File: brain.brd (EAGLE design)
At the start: 100 x 80 mm, 14 parts

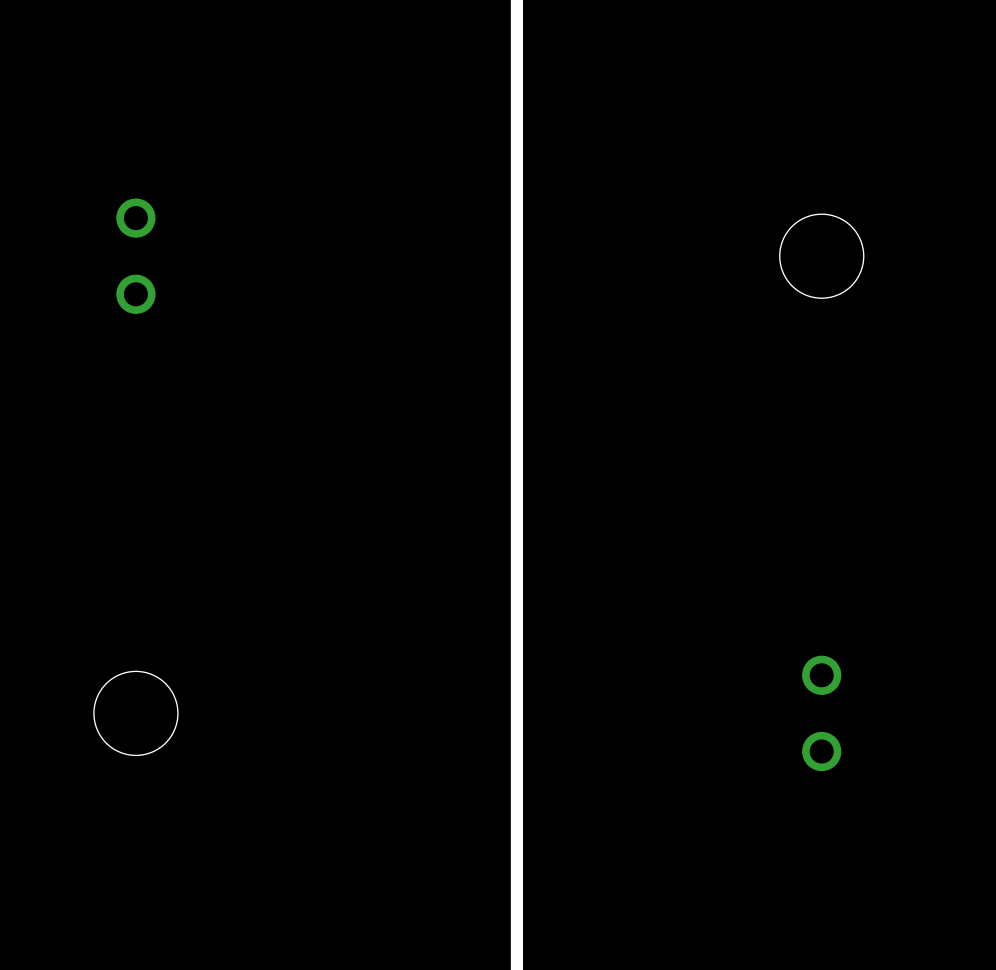
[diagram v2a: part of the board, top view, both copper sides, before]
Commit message: Added some text to board, played a bit with layout/routing.
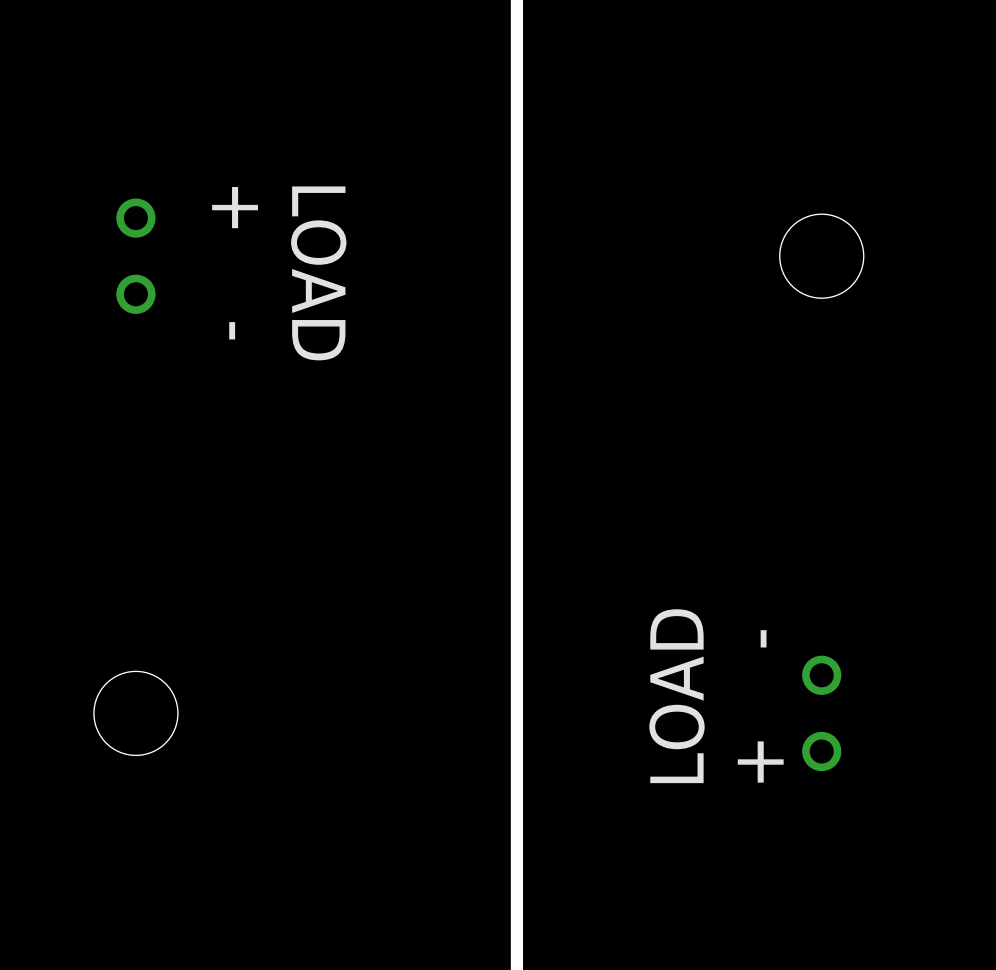
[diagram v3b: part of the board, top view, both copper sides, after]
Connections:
- removed net +3V3: U$1.8, U$2.VOUT, U$4.8, U$5.VOUT, XB1.1, XB2.1
- removed net GND: R1.2, R2.2, S1.2, S2.2, U$1.4, U$2.GND, U$3.P$2, U$4.4, U$5.GND, U$6.P$2, XB1.10, XB2.10
- removed net VIN: U$2.VIN, U$3.P$1, U$5.VIN, U$6.P$1
- new net GND1: R1.2, R2.2, S1.2, U$1.4, U$2.GND, U$3.P$2, XB1.10
- new net GND2: S2.2, U$4.4, U$5.GND, U$6.P$2, XB2.10
- new net VCC1: U$1.8, U$2.VOUT, XB1.1
- new net VIN1: U$2.VIN, U$3.P$1
- new net VIN2: U$5.VIN, U$6.P$1
- new net VOUT2: U$4.8, U$5.VOUT, XB2.1
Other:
- board text added: "LOAD + -"
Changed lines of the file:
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@@
 <setting verticaltext="up"/>
 </settings>
-<grid distance="0.05" unitdist="inch" unit="inch" style="dots" multiple="1" display="yes" altdistance="0.025" altunitdist="inch" altunit="inch"/>
+<grid distance="0.05" unitdist="inch" unit="inch" style="dots" multiple="1" display="no" altdistance="0.025" altunitdist="inch" altunit="inch"/>
 <layers>
 <layer number="1" name="Top" color="4" fill="1" visible="yes" active="yes"/>
@@
 <wire x1="49.53" y1="0" x2="50.8" y2="0" width="0.4064" layer="20"/>
 <wire x1="50.8" y1="0" x2="50.8" y2="80.01" width="0.4064" layer="20"/>
+<text x="59.69" y="31.75" size="1.778" layer="21" rot="R90">LOAD
++    -</text>
+<text x="40.64" y="52.07" size="1.778" layer="21" rot="SR270">LOAD
++    -</text>
 </plain>
 <attributes>
@@
 <param name="RoutingGrid" value="50mil"/>
 <param name="AutoGrid" value="1"/>
-<param name="Efforts" value="0"/>
+<param name="Efforts" value="1"/>
 <param name="TopRouterVariant" value="1"/>
 <param name="tpViaShape" value="round"/>
@@
 </elements>
 <signals>
-<signal name="GND">
+<signal name="N$3">
+<contactref element="R2" pad="1"/>
+<contactref element="U$1" pad="6"/>
+<contactref element="U3" pad="RING"/>
+<wire x1="90.25" y1="3.89" x2="93.345" y2="39.984" width="0" layer="19" extent="1-1"/>
+<wire x1="85.09" y1="3.81" x2="90.25" y2="3.89" width="0" layer="19" extent="1-1"/>
+</signal>
+<signal name="N$2">
+<contactref element="R1" pad="1"/>
+<contactref element="U$1" pad="7"/>
+<contactref element="U2" pad="RING"/>
+<wire x1="90.25" y1="17.86" x2="92.075" y2="39.984" width="0" layer="19" extent="1-1"/>
+<wire x1="85.09" y1="17.78" x2="90.25" y2="17.86" width="0" layer="19" extent="1-1"/>
+</signal>
+<signal name="N$4">
+<contactref element="U$1" pad="5"/>
+<contactref element="U2" pad="SLEEVE"/>
+<contactref element="U3" pad="SLEEVE"/>
+<wire x1="95.25" y1="22.86" x2="94.615" y2="39.984" width="0" layer="19" extent="1-1"/>
+<wire x1="95.25" y1="8.89" x2="95.25" y2="22.86" width="0" layer="19" extent="1-1"/>
+</signal>
+<signal name="N$11">
+<contactref element="XB1" pad="3"/>
+<contactref element="U$1" pad="3"/>
+<wire x1="93.335" y1="33.676" x2="92.63" y2="77.04" width="0" layer="19" extent="1-1"/>
+</signal>
+<signal name="N$13">
+<contactref element="XB1" pad="5"/>
+<contactref element="S1" pad="3"/>
+<wire x1="80.2894" y1="50.2412" x2="88.63" y2="77.04" width="0" layer="19" extent="1-1"/>
+</signal>
+<signal name="N$14">
+<contactref element="XB1" pad="2"/>
+<contactref element="U$1" pad="2"/>
+<wire x1="92.065" y1="33.676" x2="94.63" y2="77.04" width="0" layer="19" extent="1-1"/>
+</signal>
+<signal name="VIN2">
+<contactref element="U$5" pad="VIN"/>
+<contactref element="U$6" pad="P$1"/>
+<wire x1="26.67" y1="39.37" x2="38.1" y2="50.8" width="0" layer="19" extent="1-1"/>
+</signal>
+<signal name="N$7">
+<contactref element="XB2" pad="3"/>
+<contactref element="U$4" pad="3"/>
+<wire x1="7.7" y1="4.24" x2="6.975" y2="33.676" width="0" layer="19" extent="1-1"/>
+</signal>
+<signal name="N$8">
+<contactref element="XB2" pad="5"/>
+<contactref element="S2" pad="3"/>
+<wire x1="11.7" y1="4.24" x2="14.5288" y2="34.5694" width="0" layer="19" extent="1-1"/>
+</signal>
+<signal name="N$9">
+<contactref element="XB2" pad="2"/>
+<contactref element="U$4" pad="2"/>
+<wire x1="5.7" y1="4.24" x2="5.705" y2="33.676" width="0" layer="19" extent="1-1"/>
+</signal>
+<signal name="VOUT2">
+<contactref element="XB2" pad="1"/>
+<contactref element="U$4" pad="8"/>
+<contactref element="U$5" pad="VOUT"/>
+<wire x1="4.445" y1="39.984" x2="26.67" y2="42.164" width="0" layer="19" extent="1-1"/>
+<wire x1="3.7" y1="4.24" x2="4.445" y2="39.984" width="0" layer="19" extent="1-1"/>
+</signal>
+<signal name="GND2">
+<contactref element="XB2" pad="10"/>
+<contactref element="U$4" pad="4"/>
+<contactref element="S2" pad="2"/>
+<contactref element="U$5" pad="GND"/>
+<contactref element="U$6" pad="P$2"/>
+<wire x1="26.67" y1="40.767" x2="38.1" y2="48.26" width="0" layer="19" extent="1-1"/>
+<wire x1="21.0312" y1="39.0906" x2="26.67" y2="40.767" width="0" layer="19" extent="1-1"/>
+<wire x1="8.245" y1="33.676" x2="21.0312" y2="39.0906" width="0" layer="19" extent="1-1"/>
+<wire x1="21.7" y1="4.24" x2="8.245" y2="33.676" width="0" layer="19" extent="1-1"/>
+</signal>
+<signal name="GND1">
 <contactref element="XB1" pad="10"/>
 <contactref element="U$1" pad="4"/>
@@
 <contactref element="U$2" pad="GND"/>
 <contactref element="U$3" pad="P$2"/>
-<contactref element="XB2" pad="10"/>
-<contactref element="U$4" pad="4"/>
-<contactref element="S2" pad="2"/>
-<contactref element="U$5" pad="GND"/>
-<contactref element="U$6" pad="P$2"/>
 <wire x1="84.8106" y1="43.7388" x2="78.63" y2="77.04" width="0" layer="19" extent="1-1"/>
 <wire x1="85.09" y1="36.957" x2="84.8106" y2="43.7388" width="0" layer="19" extent="1-1"/>
@@
 <wire x1="74.93" y1="3.81" x2="74.93" y2="17.78" width="0" layer="19" extent="1-1"/>
 <wire x1="60.96" y1="35.56" x2="74.93" y2="17.78" width="0" layer="19" extent="1-1"/>
-<wire x1="8.245" y1="33.676" x2="74.93" y2="3.81" width="0" layer="19" extent="1-1"/>
-<wire x1="26.67" y1="40.767" x2="8.245" y2="33.676" width="0" layer="19" extent="1-1"/>
-<wire x1="21.0312" y1="39.0906" x2="8.245" y2="33.676" width="0" layer="19" extent="1-1"/>
-<wire x1="21.7" y1="4.24" x2="21.0312" y2="39.0906" width="0" layer="19" extent="1-1"/>
-<wire x1="38.1" y1="48.26" x2="21.7" y2="4.24" width="0" layer="19" extent="1-1"/>
-</signal>
-<signal name="N$3">
-<contactref element="R2" pad="1"/>
-<contactref element="U$1" pad="6"/>
-<contactref element="U3" pad="RING"/>
-<wire x1="85.09" y1="3.81" x2="90.25" y2="3.89" width="0" layer="19" extent="1-1"/>
-<wire x1="93.345" y1="39.984" x2="85.09" y2="3.81" width="0" layer="19" extent="1-1"/>
-</signal>
-<signal name="N$2">
-<contactref element="R1" pad="1"/>
-<contactref element="U$1" pad="7"/>
-<contactref element="U2" pad="RING"/>
-<wire x1="85.09" y1="17.78" x2="92.075" y2="39.984" width="0" layer="19" extent="1-1"/>
-<wire x1="90.25" y1="17.86" x2="85.09" y2="17.78" width="0" layer="19" extent="1-1"/>
-</signal>
-<signal name="N$4">
-<contactref element="U$1" pad="5"/>
-<contactref element="U2" pad="SLEEVE"/>
-<contactref element="U3" pad="SLEEVE"/>
-<wire x1="95.25" y1="22.86" x2="95.25" y2="8.89" width="0" layer="19" extent="1-1"/>
-<wire x1="94.615" y1="39.984" x2="95.25" y2="22.86" width="0" layer="19" extent="1-1"/>
-</signal>
-<signal name="N$11">
-<contactref element="XB1" pad="3"/>
-<contactref element="U$1" pad="3"/>
-<wire x1="93.335" y1="33.676" x2="92.63" y2="77.04" width="0" layer="19" extent="1-1"/>
-</signal>
-<signal name="N$13">
-<contactref element="XB1" pad="5"/>
-<contactref element="S1" pad="3"/>
-<wire x1="80.2894" y1="50.2412" x2="88.63" y2="77.04" width="0" layer="19" extent="1-1"/>
-</signal>
-<signal name="N$14">
-<contactref element="XB1" pad="2"/>
-<contactref element="U$1" pad="2"/>
-<wire x1="92.065" y1="33.676" x2="94.63" y2="77.04" width="0" layer="19" extent="1-1"/>
-</signal>
-<signal name="VIN">
-<contactref element="U$2" pad="VIN"/>
-<contactref element="U$3" pad="P$1"/>
-<contactref element="U$5" pad="VIN"/>
-<contactref element="U$6" pad="P$1"/>
-<wire x1="60.96" y1="33.02" x2="85.09" y2="35.56" width="0" layer="19" extent="1-1"/>
-<wire x1="38.1" y1="50.8" x2="60.96" y2="33.02" width="0" layer="19" extent="1-1"/>
-<wire x1="26.67" y1="39.37" x2="38.1" y2="50.8" width="0" layer="19" extent="1-1"/>
-</signal>
-<signal name="+3V3">
+</signal>
+<signal name="VCC1">
 <contactref element="XB1" pad="1"/>
 <contactref element="U$1" pad="8"/>
 <contactref element="U$2" pad="VOUT"/>
-<contactref element="XB2" pad="1"/>
-<contactref element="U$4" pad="8"/>
-<contactref element="U$5" pad="VOUT"/>
 <wire x1="90.805" y1="39.984" x2="96.63" y2="77.04" width="0" layer="19" extent="1-1"/>
 <wire x1="85.09" y1="38.354" x2="90.805" y2="39.984" width="0" layer="19" extent="1-1"/>
-<wire x1="3.7" y1="4.24" x2="85.09" y2="38.354" width="0" layer="19" extent="1-1"/>
-<wire x1="4.445" y1="39.984" x2="3.7" y2="4.24" width="0" layer="19" extent="1-1"/>
-<wire x1="26.67" y1="42.164" x2="4.445" y2="39.984" width="0" layer="19" extent="1-1"/>
-</signal>
-<signal name="N$7">
-<contactref element="XB2" pad="3"/>
-<contactref element="U$4" pad="3"/>
-<wire x1="7.7" y1="4.24" x2="6.975" y2="33.676" width="0" layer="19" extent="1-1"/>
-</signal>
-<signal name="N$8">
-<contactref element="XB2" pad="5"/>
-<contactref element="S2" pad="3"/>
-<wire x1="11.7" y1="4.24" x2="14.5288" y2="34.5694" width="0" layer="19" extent="1-1"/>
-</signal>
-<signal name="N$9">
-<contactref element="XB2" pad="2"/>
-<contactref element="U$4" pad="2"/>
-<wire x1="5.7" y1="4.24" x2="5.705" y2="33.676" width="0" layer="19" extent="1-1"/>
+</signal>
+<signal name="VIN1">
+<contactref element="U$2" pad="VIN"/>
+<contactref element="U$3" pad="P$1"/>
+<wire x1="60.96" y1="33.02" x2="85.09" y2="35.56" width="0" layer="19" extent="1-1"/>
 </signal>
 </signals>
 </board>
 </drawing>
+<compatibility>
+<note version="6.3" minversion="6.2.2" severity="warning">
+Since Version 6.2.2 text objects can contain more than one line,
+which will not be processed correctly with this version.
+</note>
+</compatibility>
 </eagle>

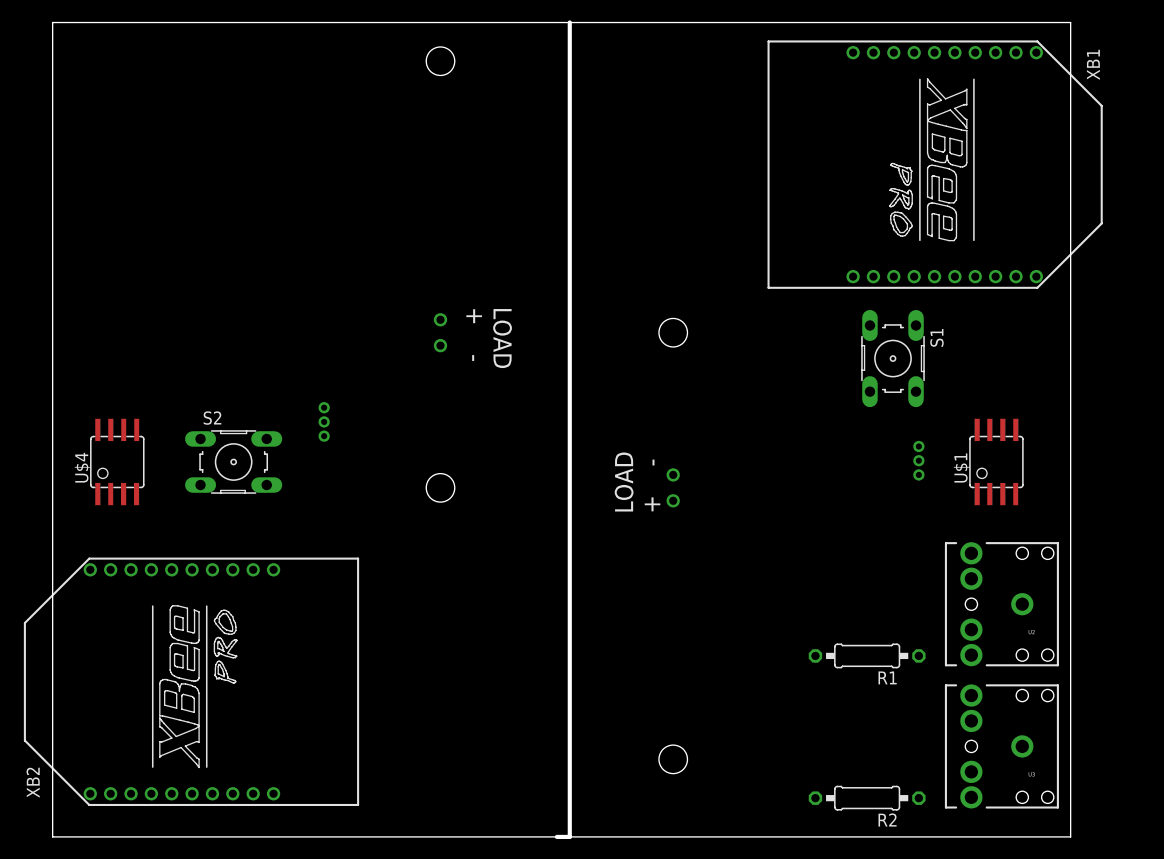
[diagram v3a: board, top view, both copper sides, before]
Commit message: Switched the ATTINY45 to the proper package. Added error LED to receiving board. Bypass capacitors added to board. To consider: using vcc/gnd planes for capacitance as well.
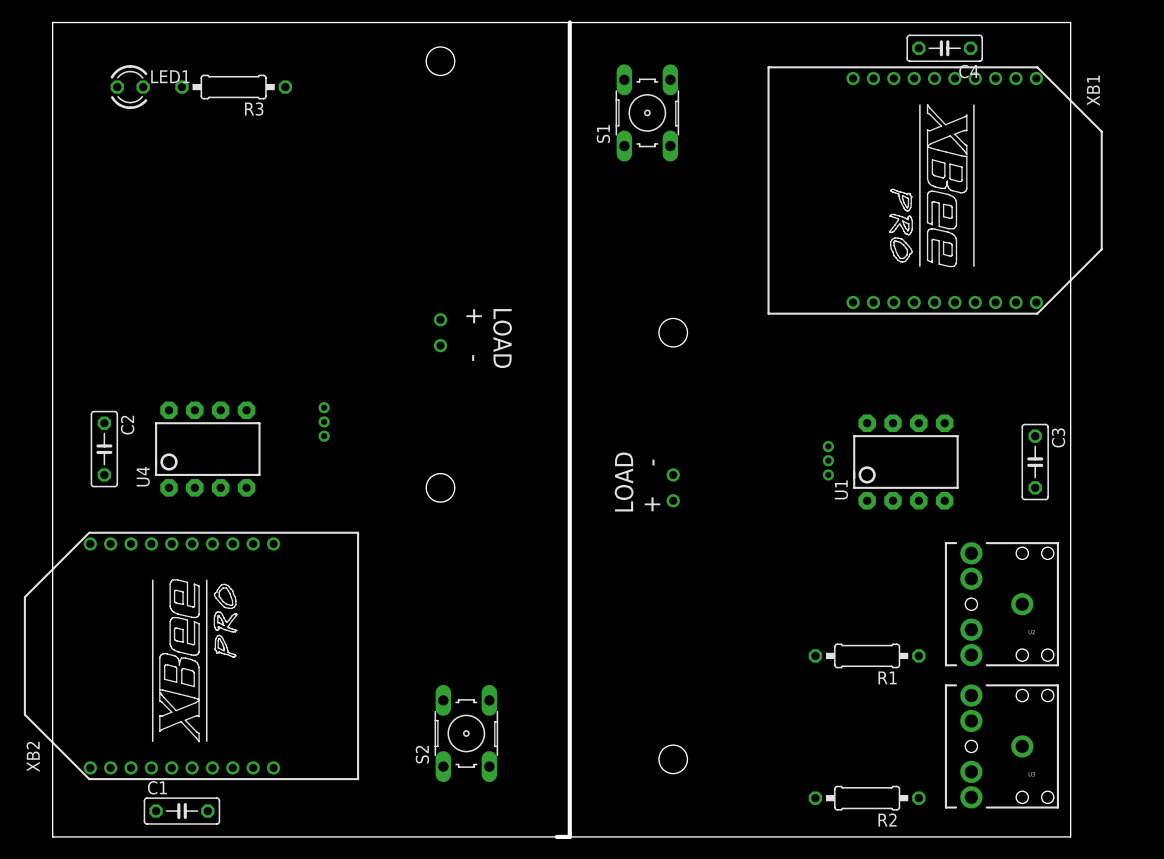
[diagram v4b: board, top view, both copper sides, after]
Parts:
- removed U$1, U$4: ATTINY45, attiny45:SOIC8
- added C1, C2, C3, C4: bypass, rcl:C050-025X075
- added LED1: ERROR, led:LED3MM
- added R3: 100, resistor:0207/10
- added U1, U4: TINY45-20-DIP, SparkFun-DigitalIC:DIP08
- moved S2 35.1 mm to (40.6, 10.2), turned to 90 degrees
- moved S1 34.1 mm to (58.4, 71.1), turned to 90 degrees
- moved U$2 8.89 mm to (76.2, 35.6)
- moved XB1 2.54 mm to (87.6, 63.5)
- moved XB2 2.54 mm to (12.7, 17.8)
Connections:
- removed net N$11: U$1.3, XB1.3
- removed net N$14: U$1.2, XB1.2
- removed net N$7: U$4.3, XB2.3
- removed net N$9: U$4.2, XB2.2
- new net N$1: LED1.A, U4.6
- new net N$5: LED1.K, R3.2
- new net RX1: U1.3, XB1.2
- new net RX2: U4.3, XB2.2
- new net TX1: U1.2, XB1.3
- new net TX2: U4.2, XB2.3
- net GND1: now also C3.2, C4.2, U1.4; no longer U$1.4
- net GND2: now also C1.2, C2.2, R3.1, U4.4; no longer U$4.4
- net N$2: now also U1.7; no longer U$1.7
- net N$3: now also U1.6; no longer U$1.6
- net N$4: now also U1.5; no longer U$1.5
- net VCC1: now also C3.1, C4.1, U1.8; no longer U$1.8
- net VOUT2: now also C1.1, C2.1, U4.8; no longer U$4.8
